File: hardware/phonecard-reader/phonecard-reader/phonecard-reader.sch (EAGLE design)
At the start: 2 parts

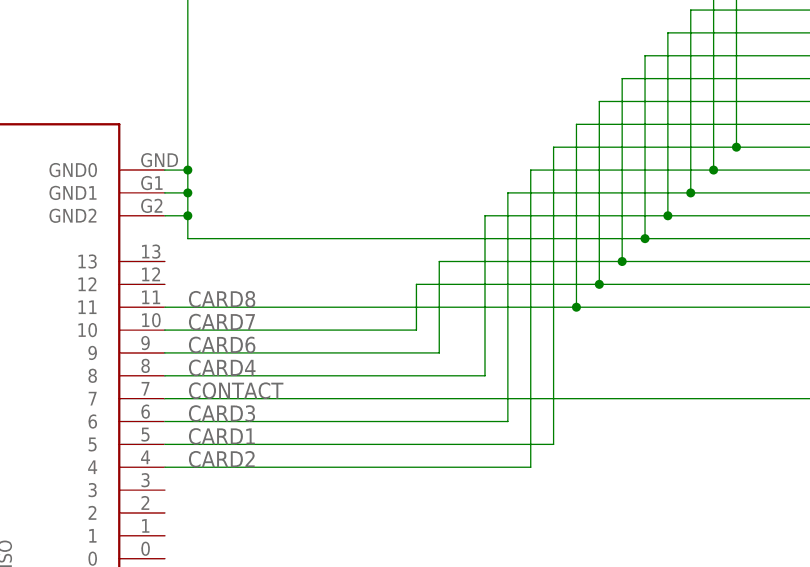
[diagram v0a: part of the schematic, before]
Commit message: feat: added azerty keyboard output jumper to pcb
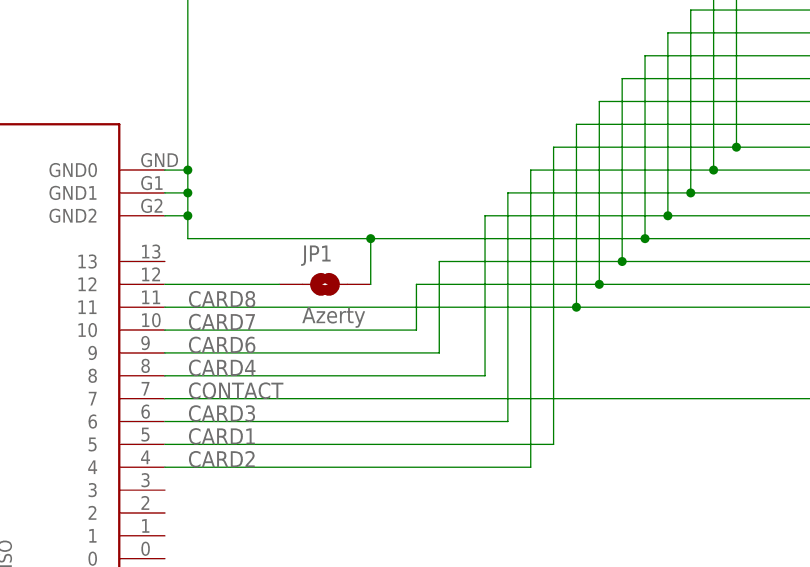
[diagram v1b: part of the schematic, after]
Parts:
- added JP1: Azerty, SparkFun-Jumpers:JUMPER-SMT_2_NO_SILK_ROUND
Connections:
- new net N$1: JP1.1, U$1.12
- net GND: now also JP1.2
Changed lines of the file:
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@@
 <layer number="48" name="Document" color="7" fill="1" visible="no" active="no"/>
 <layer number="49" name="Reference" color="7" fill="1" visible="no" active="no"/>
+<layer number="50" name="dxf" color="7" fill="1" visible="no" active="no"/>
 <layer number="51" name="tDocu" color="7" fill="1" visible="no" active="no"/>
 <layer number="52" name="bDocu" color="7" fill="1" visible="no" active="no"/>
+<layer number="53" name="tGND_GNDA" color="7" fill="9" visible="no" active="no"/>
+<layer number="54" name="bGND_GNDA" color="1" fill="9" visible="no" active="no"/>
+<layer number="56" name="wert" color="7" fill="1" visible="no" active="no"/>
+<layer number="57" name="tCAD" color="7" fill="1" visible="no" active="no"/>
+<layer number="59" name="tCarbon" color="7" fill="1" visible="no" active="no"/>
+<layer number="60" name="bCarbon" color="7" fill="1" visible="no" active="no"/>
 <layer number="88" name="SimResults" color="9" fill="1" visible="yes" active="yes"/>
 <layer number="89" name="SimProbes" color="9" fill="1" visible="yes" active="yes"/>
@@
 <layer number="97" name="Info" color="7" fill="1" visible="yes" active="yes"/>
 <layer number="98" name="Guide" color="6" fill="1" visible="yes" active="yes"/>
+<layer number="99" name="SpiceOrder" color="7" fill="1" visible="no" active="no"/>
+<layer number="100" name="Muster" color="7" fill="1" visible="no" active="no"/>
+<layer number="101" name="Patch_Top" color="12" fill="4" visible="yes" active="yes"/>
+<layer number="102" name="Vscore" color="7" fill="1" visible="yes" active="yes"/>
+<layer number="103" name="tMap" color="7" fill="1" visible="yes" active="yes"/>
+<layer number="104" name="Name" color="16" fill="1" visible="yes" active="yes"/>
+<layer number="105" name="tPlate" color="7" fill="1" visible="yes" active="yes"/>
+<layer number="106" name="bPlate" color="7" fill="1" visible="yes" active="yes"/>
+<layer number="107" name="Crop" color="7" fill="1" visible="yes" active="yes"/>
+<layer number="108" name="tplace-old" color="10" fill="1" visible="yes" active="yes"/>
+<layer number="109" name="ref-old" color="11" fill="1" visible="yes" active="yes"/>
+<layer number="110" name="fp0" color="7" fill="1" visible="yes" active="yes"/>
+<layer number="111" name="LPC17xx" color="7" fill="1" visible="yes" active="yes"/>
+<layer number="112" name="tSilk" color="7" fill="1" visible="yes" active="yes"/>
+<layer number="113" name="IDFDebug" color="7" fill="1" visible="yes" active="yes"/>
+<layer number="116" name="Patch_BOT" color="9" fill="4" visible="yes" active="yes"/>
+<layer number="118" name="Rect_Pads" color="7" fill="1" visible="yes" active="yes"/>
+<layer number="121" name="_tsilk" color="7" fill="1" visible="yes" active="yes"/>
+<layer number="122" name="_bsilk" color="7" fill="1" visible="yes" active="yes"/>
+<layer number="123" name="tTestmark" color="7" fill="1" visible="yes" active="yes"/>
+<layer number="124" name="bTestmark" color="7" fill="1" visible="yes" active="yes"/>
+<layer number="125" name="_tNames" color="7" fill="1" visible="yes" active="yes"/>
+<layer number="126" name="_bNames" color="7" fill="1" visible="yes" active="yes"/>
+<layer number="127" name="_tValues" color="7" fill="1" visible="yes" active="yes"/>
+<layer number="128" name="_bValues" color="7" fill="1" visible="yes" active="yes"/>
+<layer number="129" name="Mask" color="7" fill="1" visible="yes" active="yes"/>
+<layer number="131" name="tAdjust" color="7" fill="1" visible="yes" active="yes"/>
+<layer number="132" name="bAdjust" color="7" fill="1" visible="yes" active="yes"/>
+<layer number="144" name="Drill_legend" color="7" fill="1" visible="yes" active="yes"/>
+<layer number="150" name="Notes" color="7" fill="1" visible="yes" active="yes"/>
+<layer number="151" name="HeatSink" color="7" fill="1" visible="yes" active="yes"/>
+<layer number="152" name="_bDocu" color="7" fill="1" visible="yes" active="yes"/>
+<layer number="153" name="FabDoc1" color="7" fill="1" visible="yes" active="yes"/>
+<layer number="154" name="FabDoc2" color="7" fill="1" visible="yes" active="yes"/>
+<layer number="155" name="FabDoc3" color="7" fill="1" visible="yes" active="yes"/>
+<layer number="199" name="Contour" color="7" fill="1" visible="yes" active="yes"/>
+<layer number="200" name="200bmp" color="1" fill="10" visible="yes" active="yes"/>
+<layer number="201" name="201bmp" color="2" fill="10" visible="yes" active="yes"/>
+<layer number="202" name="202bmp" color="3" fill="10" visible="yes" active="yes"/>
+<layer number="203" name="203bmp" color="4" fill="10" visible="yes" active="yes"/>
+<layer number="204" name="204bmp" color="5" fill="10" visible="yes" active="yes"/>
+<layer number="205" name="205bmp" color="6" fill="10" visible="yes" active="yes"/>
+<layer number="206" name="206bmp" color="7" fill="10" visible="yes" active="yes"/>
+<layer number="207" name="207bmp" color="8" fill="10" visible="yes" active="yes"/>
+<layer number="208" name="208bmp" color="9" fill="10" visible="yes" active="yes"/>
+<layer number="209" name="209bmp" color="7" fill="1" visible="yes" active="yes"/>
+<layer number="210" name="210bmp" color="7" fill="1" visible="yes" active="yes"/>
+<layer number="211" name="211bmp" color="7" fill="1" visible="yes" active="yes"/>
+<layer number="212" name="212bmp" color="7" fill="1" visible="yes" active="yes"/>
+<layer number="213" name="213bmp" color="7" fill="1" visible="yes" active="yes"/>
+<layer number="214" name="214bmp" color="7" fill="1" visible="yes" active="yes"/>
+<layer number="215" name="215bmp" color="7" fill="1" visible="yes" active="yes"/>
+<layer number="216" name="216bmp" color="7" fill="1" visible="yes" active="yes"/>
+<layer number="217" name="217bmp" color="18" fill="1" visible="no" active="no"/>
+<layer number="218" name="218bmp" color="19" fill="1" visible="no" active="no"/>
+<layer number="219" name="219bmp" color="20" fill="1" visible="no" active="no"/>
+<layer number="220" name="220bmp" color="21" fill="1" visible="no" active="no"/>
+<layer number="221" name="221bmp" color="22" fill="1" visible="no" active="no"/>
+<layer number="222" name="222bmp" color="23" fill="1" visible="no" active="no"/>
+<layer number="223" name="223bmp" color="24" fill="1" visible="no" active="no"/>
+<layer number="224" name="224bmp" color="25" fill="1" visible="no" active="no"/>
+<layer number="225" name="225bmp" color="7" fill="1" visible="yes" active="yes"/>
+<layer number="226" name="226bmp" color="7" fill="1" visible="yes" active="yes"/>
+<layer number="227" name="227bmp" color="7" fill="1" visible="yes" active="yes"/>
+<layer number="228" name="228bmp" color="7" fill="1" visible="yes" active="yes"/>
+<layer number="229" name="229bmp" color="7" fill="1" visible="yes" active="yes"/>
+<layer number="230" name="230bmp" color="7" fill="1" visible="yes" active="yes"/>
+<layer number="231" name="231bmp" color="7" fill="1" visible="yes" active="yes"/>
+<layer number="248" name="Housing" color="7" fill="1" visible="yes" active="yes"/>
+<layer number="249" name="Edge" color="7" fill="1" visible="yes" active="yes"/>
+<layer number="250" name="Descript" color="3" fill="1" visible="no" active="no"/>
+<layer number="251" name="SMDround" color="12" fill="11" visible="no" active="no"/>
+<layer number="254" name="cooling" color="7" fill="1" visible="yes" active="yes"/>
+<layer number="255" name="routoute" color="7" fill="1" visible="yes" active="yes"/>
 </layers>
 <schematic xreflabel="%F%N/%S.%C%R" xrefpart="/%S.%C%R">
@@
 <part name="U$1" library="mylibrary" library_urn="urn:adsk.eagle:library:25379741" deviceset="ITSY_BITSY" device=""/>
 <part name="U$2" library="mylibrary" library_urn="urn:adsk.eagle:library:25379741" deviceset="7312P0235A13LFC" device="" package3d_urn="urn:adsk.eagle:package:25379743/2"/>
+<part name="JP1" library="SparkFun-Jumpers" library_urn="urn:adsk.eagle:library:528" deviceset="JUMPER-SMT_2_NO" device="_SILK_ROUND" package3d_urn="urn:adsk.eagle:package:39280/1" value="Azerty"/>
 </parts>
 <sheets>
@@
 <instance part="U$1" gate="G$1" x="12.7" y="53.34" smashed="yes"/>
 <instance part="U$2" gate="G$1" x="157.48" y="55.88" smashed="yes"/>
+<instance part="JP1" gate="G$1" x="83.82" y="38.1" smashed="yes">
+<attribute name="NAME" x="81.28" y="40.64" size="1.778" layer="95" font="vector"/>
+<attribute name="VALUE" x="81.28" y="35.56" size="1.778" layer="96" font="vector" align="top-left"/>
+</instance>
 </instances>
 <busses>
@@
 <pinref part="U$2" gate="G$1" pin="F5"/>
 <wire x1="119.38" y1="43.18" x2="139.7" y2="43.18" width="0.1524" layer="91"/>
-<wire x1="119.38" y1="43.18" x2="68.58" y2="43.18" width="0.1524" layer="91"/>
+<wire x1="119.38" y1="43.18" x2="88.9" y2="43.18" width="0.1524" layer="91"/>
 <junction x="119.38" y="43.18"/>
 <pinref part="U$1" gate="G$1" pin="GND2"/>
+<wire x1="88.9" y1="43.18" x2="68.58" y2="43.18" width="0.1524" layer="91"/>
 <wire x1="66.04" y1="45.72" x2="68.58" y2="45.72" width="0.1524" layer="91"/>
 <wire x1="68.58" y1="45.72" x2="68.58" y2="48.26" width="0.1524" layer="91"/>
@@
 <junction x="68.58" y="45.72"/>
 <label x="78.74" y="81.28" size="1.778" layer="95"/>
+<pinref part="JP1" gate="G$1" pin="2"/>
+<wire x1="88.9" y1="38.1" x2="88.9" y2="43.18" width="0.1524" layer="91"/>
+<junction x="88.9" y="43.18"/>
 </segment>
 </net>
@@
 </segment>
 </net>
+<net name="N$1" class="0">
+<segment>
+<pinref part="U$1" gate="G$1" pin="12"/>
+<pinref part="JP1" gate="G$1" pin="1"/>
+<wire x1="66.04" y1="38.1" x2="78.74" y2="38.1" width="0.1524" layer="91"/>
+</segment>
+</net>

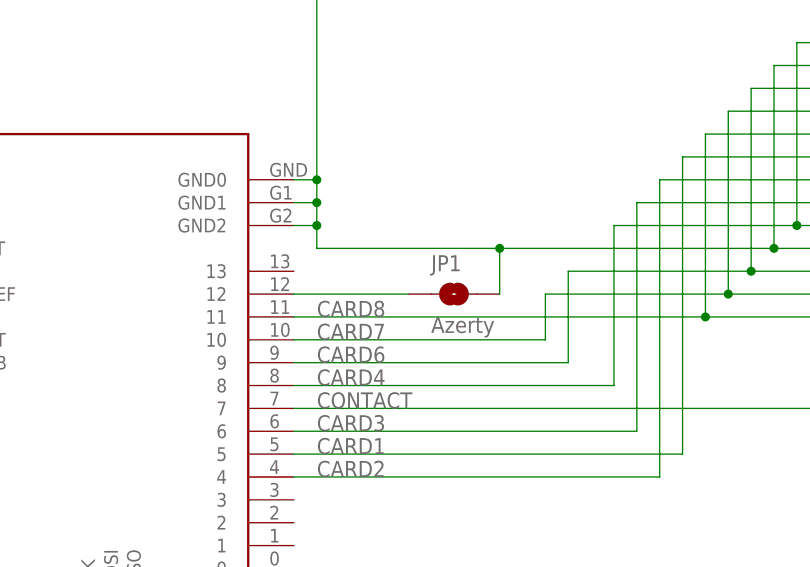
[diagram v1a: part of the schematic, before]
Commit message: feat: update keyboard switch pin
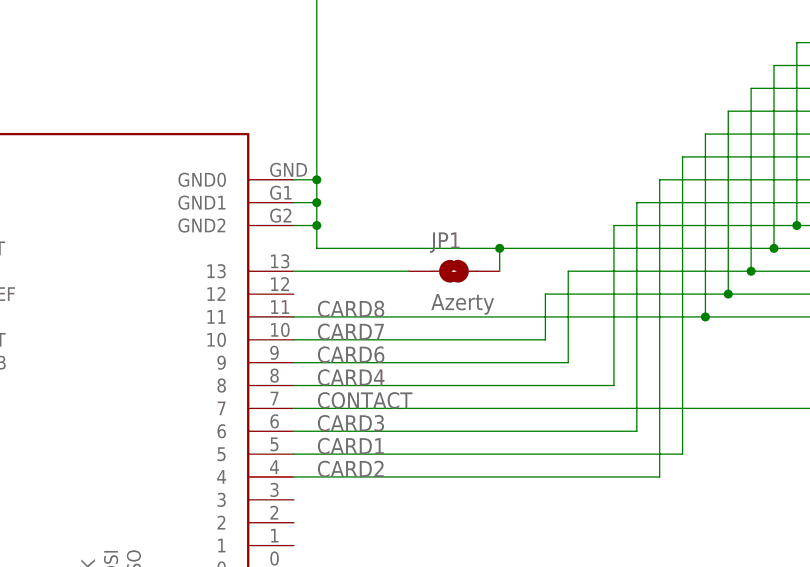
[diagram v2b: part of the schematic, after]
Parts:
- U$1: value (none) -> Itsy Bitsy 5V
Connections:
- net N$1: now also U$1.13; no longer U$1.12
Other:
- moved on the sheet: JP1
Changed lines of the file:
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@@
 </classes>
 <parts>
-<part name="U$1" library="mylibrary" library_urn="urn:adsk.eagle:library:25379741" deviceset="ITSY_BITSY" device=""/>
+<part name="U$1" library="mylibrary" library_urn="urn:adsk.eagle:library:25379741" deviceset="ITSY_BITSY" device="" value="Itsy Bitsy 5V"/>
 <part name="U$2" library="mylibrary" library_urn="urn:adsk.eagle:library:25379741" deviceset="7312P0235A13LFC" device="" package3d_urn="urn:adsk.eagle:package:25379743/2"/>
 <part name="JP1" library="SparkFun-Jumpers" library_urn="urn:adsk.eagle:library:528" deviceset="JUMPER-SMT_2_NO" device="_SILK_ROUND" package3d_urn="urn:adsk.eagle:package:39280/1" value="Azerty"/>
@@
 <instance part="U$1" gate="G$1" x="12.7" y="53.34" smashed="yes"/>
 <instance part="U$2" gate="G$1" x="157.48" y="55.88" smashed="yes"/>
-<instance part="JP1" gate="G$1" x="83.82" y="38.1" smashed="yes">
-<attribute name="NAME" x="81.28" y="40.64" size="1.778" layer="95" font="vector"/>
-<attribute name="VALUE" x="81.28" y="35.56" size="1.778" layer="96" font="vector" align="top-left"/>
+<instance part="JP1" gate="G$1" x="83.82" y="40.64" smashed="yes">
+<attribute name="NAME" x="81.28" y="43.18" size="1.778" layer="95" font="vector"/>
+<attribute name="VALUE" x="81.28" y="38.1" size="1.778" layer="96" font="vector" align="top-left"/>
 </instance>
 </instances>
@@
 <label x="78.74" y="81.28" size="1.778" layer="95"/>
 <pinref part="JP1" gate="G$1" pin="2"/>
-<wire x1="88.9" y1="38.1" x2="88.9" y2="43.18" width="0.1524" layer="91"/>
+<wire x1="88.9" y1="40.64" x2="88.9" y2="43.18" width="0.1524" layer="91"/>
 <junction x="88.9" y="43.18"/>
 </segment>
@@
 <net name="N$1" class="0">
 <segment>
-<pinref part="U$1" gate="G$1" pin="12"/>
+<pinref part="U$1" gate="G$1" pin="13"/>
 <pinref part="JP1" gate="G$1" pin="1"/>
-<wire x1="66.04" y1="38.1" x2="78.74" y2="38.1" width="0.1524" layer="91"/>
+<wire x1="66.04" y1="40.64" x2="78.74" y2="40.64" width="0.1524" layer="91"/>
 </segment>
 </net>
